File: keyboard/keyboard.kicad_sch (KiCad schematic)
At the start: 64 parts, among them SW1 MX_SW_HS, SW10 MX_SW_HS, SW11 MX_SW_HS, SW12 MX_SW_HS, SW13 MX_SW_HS, SW14 MX_SW_HS, SW15 MX_SW_HS, SW16 MX_SW_HS, SW17 MX_SW_HS, SW18 MX_SW_HS, SW19 MX_SW_HS, SW2 MX_SW_HS, SW20 MX_SW_HS, SW21 MX_SW_HS, SW22 MX_SW_HS, SW23 MX_SW_HS, SW24 MX_SW_HS, SW25 MX_SW_HS, SW26 MX_SW_HS, SW27 MX_SW_HS, SW28 MX_SW_HS, SW29 MX_SW_HS, SW3 MX_SW_HS, SW30 MX_SW_HS, SW31 MX_SW_HS, SW32 MX_SW_HS, SW33 MX_SW_HS, SW34 MX_SW_HS, SW35 MX_SW_HS, SW36 MX_SW_HS, SW37 MX_SW_HS, SW38 MX_SW_HS, SW39 MX_SW_HS, SW4 MX_SW_HS, SW40 MX_SW_HS, SW41 MX_SW_HS, SW42 MX_SW_HS, SW43 MX_SW_HS, SW44 MX_SW_HS, SW45 MX_SW_HS, SW46 MX_SW_HS, SW47 MX_SW_HS, SW48 MX_SW_HS, SW49 MX_SW_HS, SW5 MX_SW_HS, SW50 MX_SW_HS, SW51 MX_SW_HS, SW52 MX_SW_HS, SW53 MX_SW_HS, SW54 MX_SW_HS, SW55 MX_SW_HS, SW56 MX_SW_HS, SW57 MX_SW_HS, SW58 MX_SW_HS, SW59 MX_SW_HS, SW6 MX_SW_HS, SW60 MX_SW_HS, SW61 MX_SW_HS, SW62 MX_SW_HS, SW63 MX_SW_HS, SW64 MX_SW_HS, SW7 MX_SW_HS, SW8 MX_SW_HS, SW9 MX_SW_HS

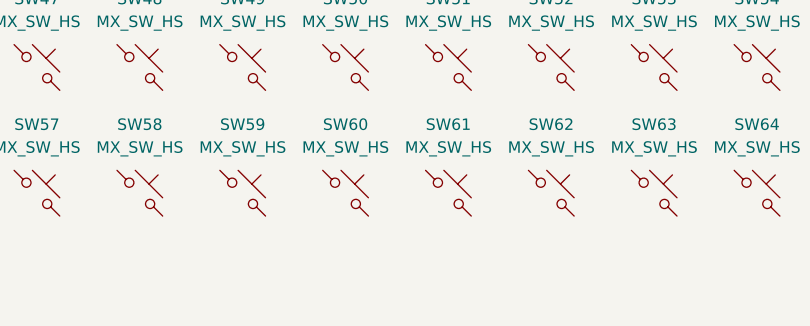
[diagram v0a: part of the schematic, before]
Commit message: Add stabiliser
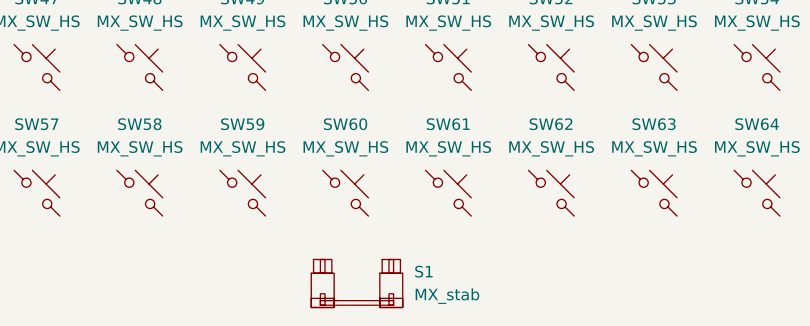
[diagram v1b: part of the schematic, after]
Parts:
- added S1: MX_stab, marbastlib-mx:STAB_MX_P_2u, symbol marbastlib-mx:MX_stab
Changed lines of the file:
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@@
     (pin "2")
+  )
+  (symbol (lib_id "marbastlib-mx:MX_stab") (at 167.64 134.62 0) (unit 1)
+    (in_bom yes) (on_board yes) (fields_autoplaced)
+    (property "Reference" "S1" (id 0) (at 173.99 133.2229 0)
+      (effects (font (size 1.27 1.27)) (justify left))
+    )
+    (property "Value" "MX_stab" (id 1) (at 173.99 135.7629 0)
+      (effects (font (size 1.27 1.27)) (justify left))
+    )
+    (property "Footprint" "marbastlib-mx:STAB_MX_P_2u" (id 2) (at 167.64 134.62 0)
+      (effects (font (size 1.27 1.27)) hide)
+    )
+    (property "Datasheet" "" (id 3) (at 167.64 134.62 0)
+      (effects (font (size 1.27 1.27)) hide)
+    )
   )
   (symbol (lib_id "marbastlib-mx:MX_SW_HS") (at 166.37 96.52 0) (unit 1)
@@
   )
   (symbol_instances
+    (path "/ac301bbf-d79a-4cf3-be1f-db1ba96ac744"
+      (reference "S1") (unit 1) (value "MX_stab") (footprint "marbastlib-mx:STAB_MX_P_2u")
+    )
     (path "/eb620e2f-3e85-4213-a7f2-d81d6fb14972"
       (reference "SW1") (unit 1) (value "MX_SW_HS") (footprint "marbastlib-mx:SW_MX_HS_1u")

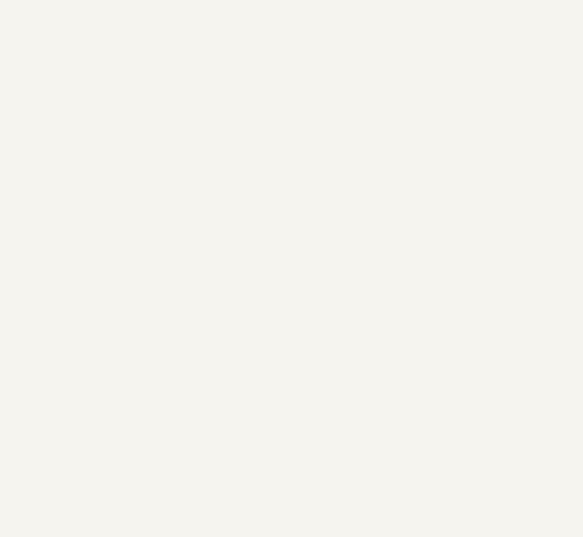
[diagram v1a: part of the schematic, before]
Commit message: Add the Keebio symbols and footprints, and add a Pro Micro to the PCB
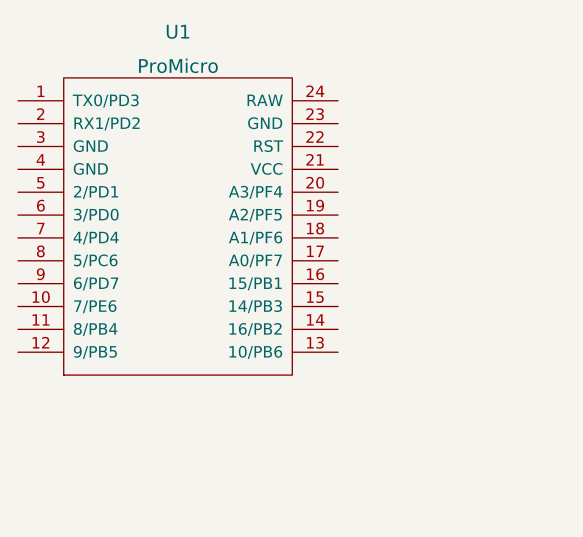
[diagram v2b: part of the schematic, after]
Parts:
- added U1: ProMicro, symbol keebio:ProMicro
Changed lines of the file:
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@@
     (pin "2")
+  )
+  (symbol (lib_id "keebio:ProMicro") (at 49.53 62.23 0) (unit 1)
+    (in_bom yes) (on_board yes) (fields_autoplaced)
+    (property "Reference" "U1" (id 0) (at 49.53 40.64 0)
+      (effects (font (size 1.524 1.524)))
+    )
+    (property "Value" "ProMicro" (id 1) (at 49.53 44.45 0)
+      (effects (font (size 1.524 1.524)))
+    )
+    (property "Footprint" "" (id 2) (at 76.2 125.73 90)
+      (effects (font (size 1.524 1.524)) hide)
+    )
+    (property "Datasheet" "" (id 3) (at 76.2 125.73 90)
+      (effects (font (size 1.524 1.524)) hide)
+    )
+    (pin "1")
+    (pin "10")
+    (pin "11")
+    (pin "12")
+    (pin "13")
+    (pin "14")
+    (pin "15")
+    (pin "16")
+    (pin "17")
+    (pin "18")
+    (pin "19")
+    (pin "2")
+    (pin "20")
+    (pin "21")
+    (pin "22")
+    (pin "23")
+    (pin "24")
+    (pin "3")
+    (pin "4")
+    (pin "5")
+    (pin "6")
+    (pin "7")
+    (pin "8")
+    (pin "9")
   )
   (symbol (lib_id "marbastlib-mx:MX_SW_HS") (at 200.66 82.55 0) (unit 1)
@@
       (reference "SW64") (unit 1) (value "MX_SW_HS") (footprint "marbastlib-mx:SW_MX_HS_1u")
     )
-  )
+    (path "/47c07748-ef56-4fbc-bc04-a64b7175dd55"
+      (reference "U1") (unit 1) (value "ProMicro") (footprint "")
+    )
+  )

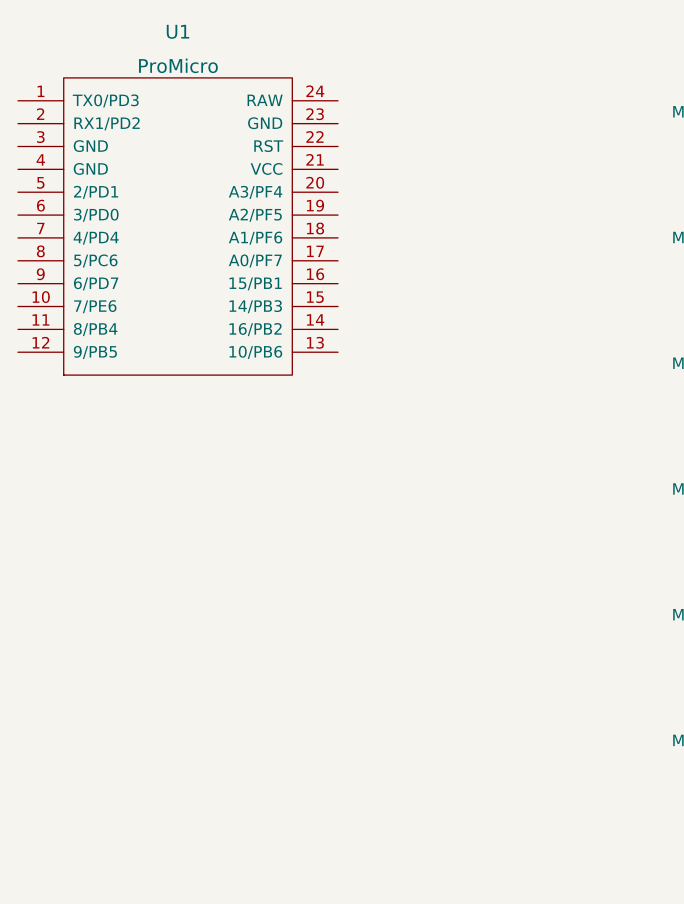
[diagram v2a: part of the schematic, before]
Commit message: Add the reset switch
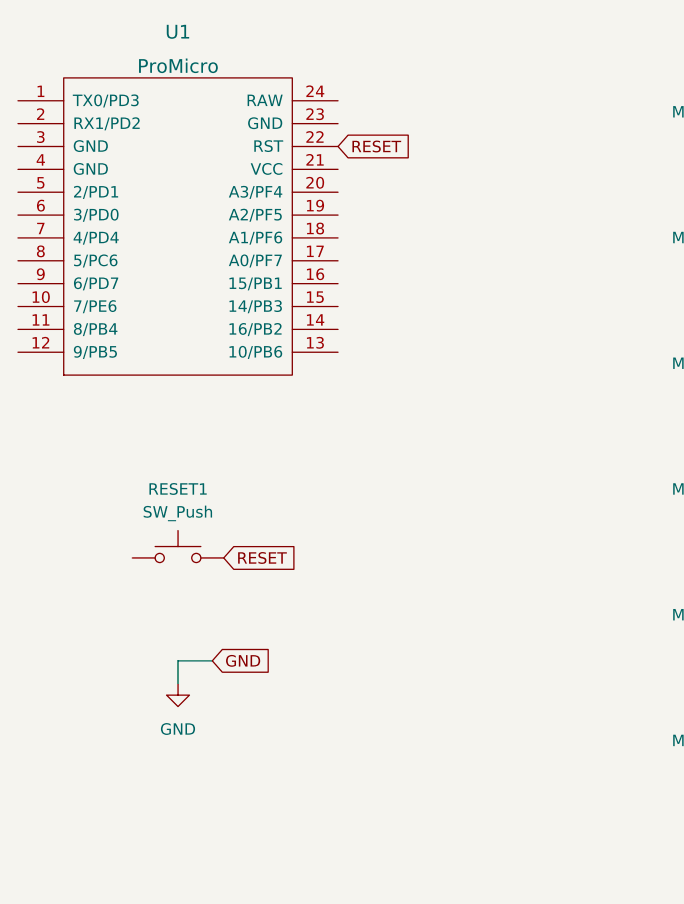
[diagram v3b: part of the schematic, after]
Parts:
- added RESET1: SW_Push, Button_Switch_THT:SW_PUSH_6mm_H13mm, symbol Switch:SW_Push
- U1: footprint (none) -> Keebio-Parts:ArduinoProMicro
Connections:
- net RESET: now reaches U1.22 (RST)
- net RESET: now also RESET1.2
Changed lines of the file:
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@@
 (kicad_sch (version 20211123) (generator eeschema)
   (paper "A4")
+  (wire (pts (xy 49.53 113.03) (xy 49.53 110.49))
+    (stroke (width 0) (type default) (color 0 0 0 0))
+  )
+  (wire (pts (xy 49.53 110.49) (xy 53.34 110.49))
+    (stroke (width 0) (type default) (color 0 0 0 0))
+  )
+  (global_label "GND" (shape input) (at 53.34 110.49 0) (fields_autoplaced)
+    (effects (font (size 1.27 1.27)) (justify left))
+    (property "Intersheet References" "${INTERSHEET_REFS}" (id 0) (at 59.6236 110.4106 0)
+      (effects (font (size 1.27 1.27)) (justify left) hide)
+    )
+  )
+  (global_label "RESET" (shape input) (at 54.61 99.06 0) (fields_autoplaced)
+    (effects (font (size 1.27 1.27)) (justify left))
+    (property "Intersheet References" "${INTERSHEET_REFS}" (id 0) (at 62.7683 98.9806 0)
+      (effects (font (size 1.27 1.27)) (justify left) hide)
+    )
+  )
+  (global_label "RESET" (shape input) (at 67.31 53.34 0) (fields_autoplaced)
+    (effects (font (size 1.27 1.27)) (justify left))
+    (property "Intersheet References" "${INTERSHEET_REFS}" (id 0) (at 75.4683 53.2606 0)
+      (effects (font (size 1.27 1.27)) (justify left) hide)
+    )
+  )
   (symbol (lib_id "marbastlib-mx:MX_SW_HS") (at 177.8 68.58 0) (unit 1)
     (in_bom yes) (on_board yes) (fields_autoplaced)
@@
     (pin "2")
   )
+  (symbol (lib_id "power:GND") (at 49.53 113.03 0) (unit 1)
+    (in_bom yes) (on_board yes) (fields_autoplaced)
+    (property "Reference" "#PWR0101" (id 0) (at 49.53 119.38 0)
+      (effects (font (size 1.27 1.27)) hide)
+    )
+    (property "Value" "GND" (id 1) (at 49.53 118.11 0))
+    (property "Footprint" "" (id 2) (at 49.53 113.03 0)
+      (effects (font (size 1.27 1.27)) hide)
+    )
+    (property "Datasheet" "" (id 3) (at 49.53 113.03 0)
+      (effects (font (size 1.27 1.27)) hide)
+    )
+    (pin "1")
+  )
   (symbol (lib_id "marbastlib-mx:MX_SW_HS") (at 212.09 96.52 0) (unit 1)
     (in_bom yes) (on_board yes) (fields_autoplaced)
@@
       (effects (font (size 1.524 1.524)))
     )
-    (property "Footprint" "" (id 2) (at 76.2 125.73 90)
+    (property "Footprint" "Keebio-Parts:ArduinoProMicro" (id 2) (at 76.2 125.73 90)
       (effects (font (size 1.524 1.524)) hide)
     )
@@
     (pin "2")
   )
+  (symbol (lib_id "Switch:SW_Push") (at 49.53 99.06 0) (unit 1)
+    (in_bom yes) (on_board yes) (fields_autoplaced)
+    (property "Reference" "RESET1" (id 0) (at 49.53 91.44 0))
+    (property "Value" "SW_Push" (id 1) (at 49.53 93.98 0))
+    (property "Footprint" "Button_Switch_THT:SW_PUSH_6mm_H13mm" (id 2) (at 49.53 93.98 0)
+      (effects (font (size 1.27 1.27)) hide)
+    )
+    (property "Datasheet" "~" (id 3) (at 49.53 93.98 0)
+      (effects (font (size 1.27 1.27)) hide)
+    )
+    (pin "1")
+    (pin "2")
+  )
   (symbol (lib_id "marbastlib-mx:MX_SW_HS") (at 200.66 54.61 0) (unit 1)
     (in_bom yes) (on_board yes) (fields_autoplaced)
@@
   )
   (symbol_instances
+    (path "/0fc0bad5-96f3-4074-96e7-a3047f49a715"
+      (reference "#PWR0101") (unit 1) (value "GND") (footprint "")
+    )
+    (path "/69aaefbf-88d4-415d-ad96-2a6ff3ee3a2f"
+      (reference "RESET1") (unit 1) (value "SW_Push") (footprint "Button_Switch_THT:SW_PUSH_6mm_H13mm")
+    )
     (path "/ac301bbf-d79a-4cf3-be1f-db1ba96ac744"
       (reference "S1") (unit 1) (value "MX_stab") (footprint "marbastlib-mx:STAB_MX_P_2u")
@@
     )
     (path "/47c07748-ef56-4fbc-bc04-a64b7175dd55"
-      (reference "U1") (unit 1) (value "ProMicro") (footprint "")
-    )
-  )
+      (reference "U1") (unit 1) (value "ProMicro") (footprint "Keebio-Parts:ArduinoProMicro")
+    )
+  )

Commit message: Add the diodes
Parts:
- added D1, D10, D11, D12, D13, D14, D15, D16, D17, D18, D19, D2, D20, D21, D22, D23, D24, D25, D26, D27, D28, D29, D3, D30, D31, D32, D33, D34, D35, D36, D37, D38, D39, D4, D40, D41, D42, D43, D44, D45, D46, D47, D48, D49, D5, D50, D51, D52, D53, D54, D55, D56, D57, D58, D59, D6, D60, D61, D62, D63, D64, D7, D8, D9: 1N4148, Diode_THT:D_DO-35_SOD27_P7.62mm_Horizontal, symbol Diode:1N4148
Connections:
- net at SW18.1: now also D18.2 (A)
- net at SW23.1: now also D23.2 (A)
- net at SW14.1: now also D14.2 (A)
- net at SW26.1: now also D26.2 (A)
- net at SW43.1: now also D43.2 (A)
- net at SW3.1: now also D3.2 (A)
- net at SW48.1: now also D48.2 (A)
- net at SW49.1: now also D49.2 (A)
- net at SW17.1: now also D17.2 (A)
- net at SW54.1: now also D54.2 (A)
- net at SW58.1: now also D58.2 (A)
- net at SW21.1: now also D21.2 (A)
- net at SW19.1: now also D19.2 (A)
- net at SW15.1: now also D15.2 (A)
- net at SW46.1: now also D46.2 (A)
- net at SW25.1: now also D25.2 (A)
- net at SW13.1: now also D13.2 (A)
- net at SW31.1: now also D31.2 (A)
- net at SW63.1: now also D63.2 (A)
- net at SW30.1: now also D30.2 (A)
- net at SW20.1: now also D20.2 (A)
- net at SW51.1: now also D51.2 (A)
- net at SW35.1: now also D35.2 (A)
- net at SW50.1: now also D50.2 (A)
- net at SW41.1: now also D41.2 (A)
- net at SW53.1: now also D53.2 (A)
- net at SW9.1: now also D9.2 (A)
- net at SW59.1: now also D59.2 (A)
- net at SW6.1: now also D6.2 (A)
- net at SW62.1: now also D62.2 (A)
- net at SW24.1: now also D24.2 (A)
- net at SW42.1: now also D42.2 (A)
- net at SW37.1: now also D37.2 (A)
- net at SW34.1: now also D34.2 (A)
- net at SW28.1: now also D28.2 (A)
- net at SW40.1: now also D40.2 (A)
- net at SW11.1: now also D11.2 (A)
- net at SW22.1: now also D22.2 (A)
- net at SW60.1: now also D60.2 (A)
- net at SW47.1: now also D47.2 (A)
- net at SW38.1: now also D38.2 (A)
- net at SW39.1: now also D39.2 (A)
- net at SW55.1: now also D55.2 (A)
- net at SW64.1: now also D64.2 (A)
- net at SW12.1: now also D12.2 (A)
- net at SW16.1: now also D16.2 (A)
- net at SW33.1: now also D33.2 (A)
- net at SW56.1: now also D56.2 (A)
- net at SW45.1: now also D45.2 (A)
- net at SW5.1: now also D5.2 (A)
- net at SW57.1: now also D57.2 (A)
- net at SW4.1: now also D4.2 (A)
- net at SW10.1: now also D10.2 (A)
- net at SW32.1: now also D32.2 (A)
- net at SW29.1: now also D29.2 (A)
- net at SW36.1: now also D36.2 (A)
- net at SW2.1: now also D2.2 (A)
- net at SW61.1: now also D61.2 (A)
- net at SW44.1: now also D44.2 (A)
- net at SW27.1: now also D27.2 (A)
- net at SW7.1: now also D7.2 (A)
- net at SW1.1: now also D1.2 (A)
- net at SW8.1: now also D8.2 (A)
- net at SW52.1: now also D52.2 (A)
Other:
- moved on the sheet: RESET1, S1, SW1, SW10, SW11, SW12, SW13, SW14, SW15, SW16, SW17, SW18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

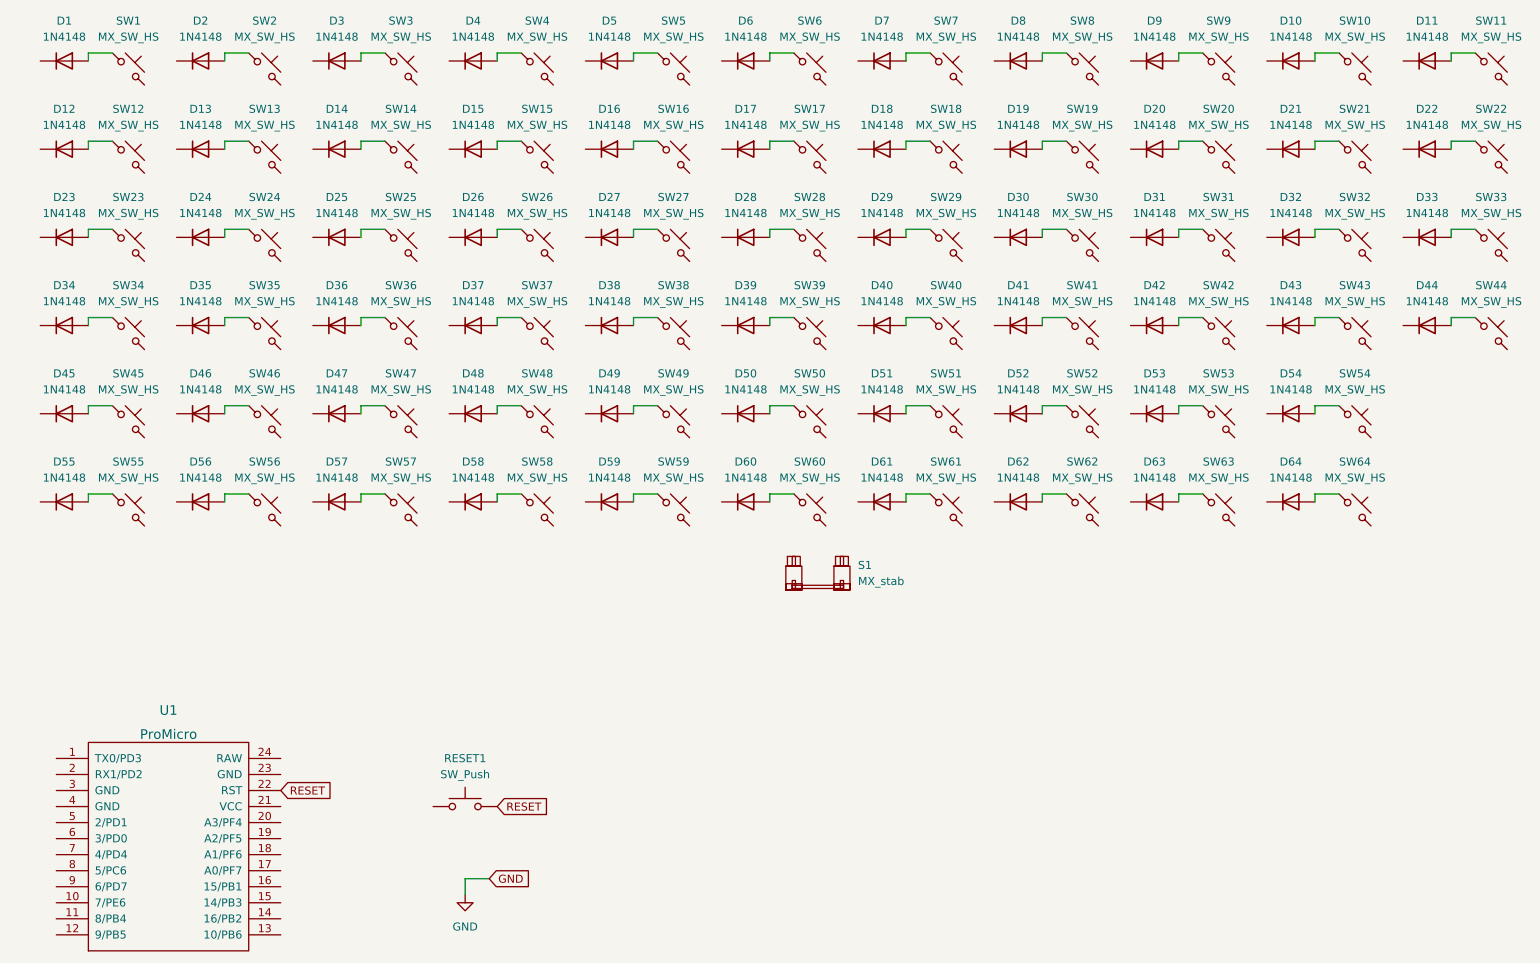
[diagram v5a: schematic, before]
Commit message: Wire up the rows and columns in the schematic
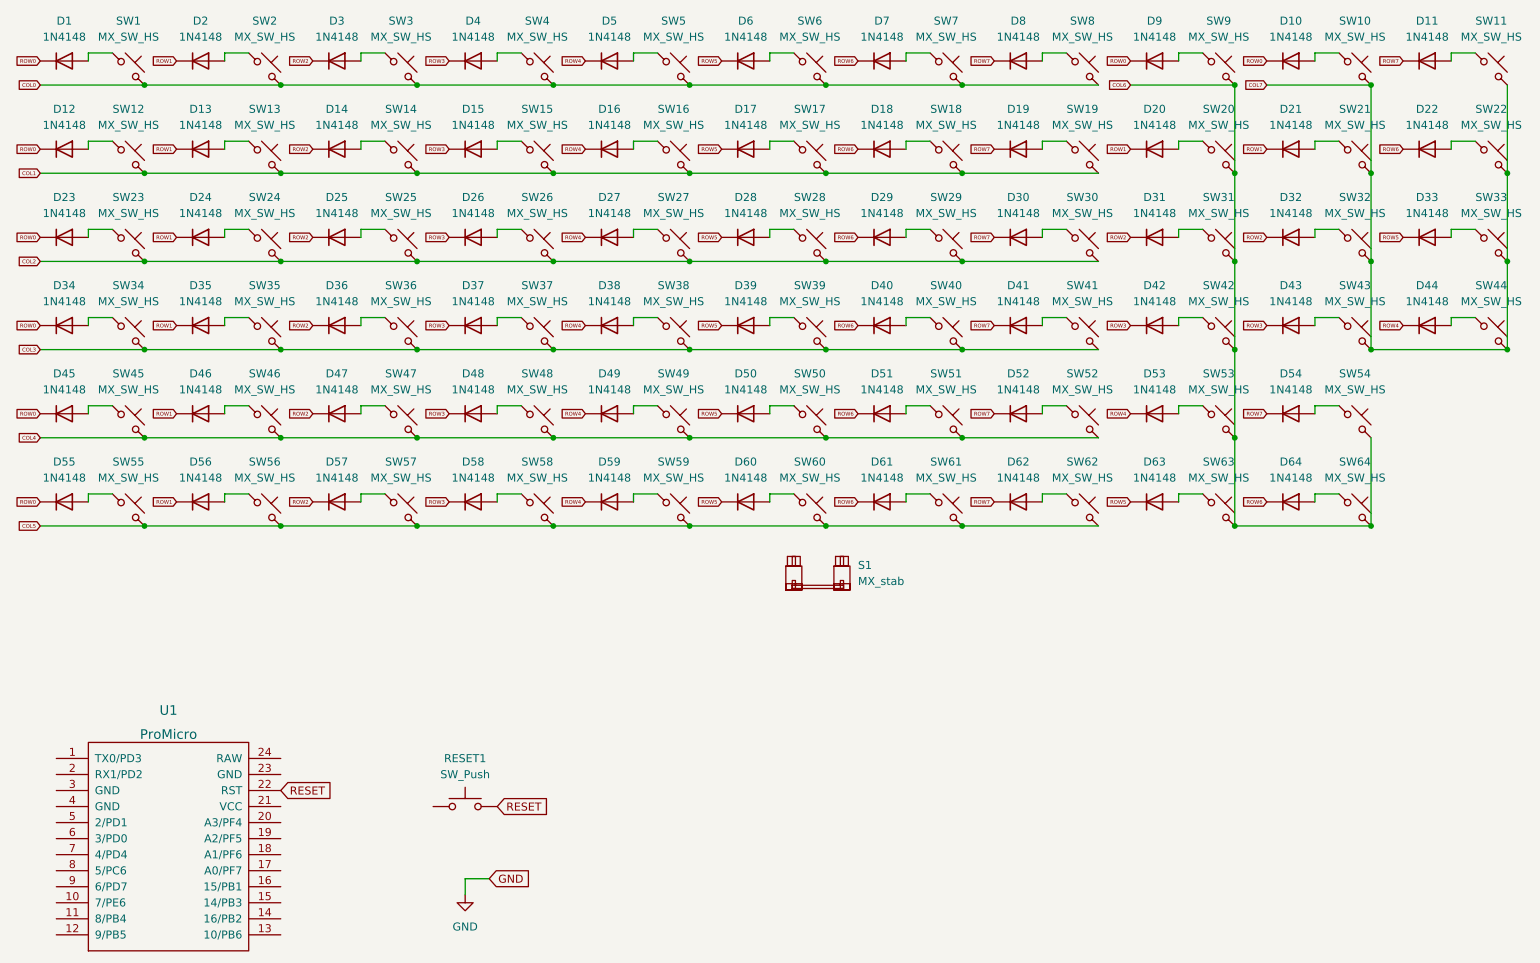
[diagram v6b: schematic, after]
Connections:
- net ROW7: now reaches D11.1 (K)
- net ROW7: now also D19.1 (K), D30.1 (K), D41.1 (K), D52.1 (K), D54.1 (K), D62.1 (K), D8.1 (K)
- net COL1: now reaches SW18.2
- net COL1: now also SW12.2, SW13.2, SW14.2, SW15.2, SW16.2, SW17.2, SW19.2
- net ROW2: now reaches D32.1 (K)
- net ROW2: now also D14.1 (K), D25.1 (K), D3.1 (K), D31.1 (K), D36.1 (K), D47.1 (K), D57.1 (K)
- net COL2: now reaches SW23.2
- net COL2: now also SW24.2, SW25.2, SW26.2, SW27.2, SW28.2, SW29.2, SW30.2
- net ROW4: now reaches D49.1 (K)
- net ROW4: now also D16.1 (K), D27.1 (K), D38.1 (K), D44.1 (K), D5.1 (K), D53.1 (K), D59.1 (K)
- net COL7: now reaches SW43.2
- net COL7: now also SW10.2, SW11.2, SW21.2, SW22.2, SW32.2, SW33.2, SW44.2
- net COL0: now reaches SW3.2
- net COL0: now also SW1.2, SW2.2, SW4.2, SW5.2, SW6.2, SW7.2, SW8.2
- net ROW0: now reaches D55.1 (K)
- net ROW0: now also D1.1 (K), D10.1 (K), D12.1 (K), D23.1 (K), D34.1 (K), D45.1 (K), D9.1 (K)
- net COL4: now reaches SW48.2
- net COL4: now also SW45.2, SW46.2, SW47.2, SW49.2, SW50.2, SW51.2, SW52.2
- net ROW3: now reaches D26.1 (K)
- net ROW3: now also D15.1 (K), D37.1 (K), D4.1 (K), D42.1 (K), D43.1 (K), D48.1 (K), D58.1 (K)
- net ROW6: now reaches D7.1 (K)
- net ROW6: now also D18.1 (K), D22.1 (K), D29.1 (K), D40.1 (K), D51.1 (K), D61.1 (K), D64.1 (K)
- net COL6: now reaches SW54.2
- net COL6: now also SW20.2, SW31.2, SW42.2, SW53.2, SW63.2, SW64.2, SW9.2
- net COL5: now reaches SW58.2
- net COL5: now also SW55.2, SW56.2, SW57.2, SW59.2, SW60.2, SW61.2, SW62.2
- net ROW1: now reaches D56.1 (K)
- net ROW1: now also D13.1 (K), D2.1 (K), D20.1 (K), D21.1 (K), D24.1 (K), D35.1 (K), D46.1 (K)
- net ROW5: now reaches D50.1 (K)
- net ROW5: now also D17.1 (K), D28.1 (K), D33.1 (K), D39.1 (K), D6.1 (K), D60.1 (K), D63.1 (K)
- net COL3: now reaches SW35.2
- net COL3: now also SW34.2, SW36.2, SW37.2, SW38.2, SW39.2, SW40.2, SW41.2
